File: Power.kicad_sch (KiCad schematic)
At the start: 18 parts, among them J4 Conn_01x02, SW2 SW_Push, U6 NPM1300-QEAA-R7

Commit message: Layout V1
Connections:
- net VSET2: now reaches R13.1, U6.16 (VSET2)
- net VSET1: now reaches R12.1, U6.17 (VSET1)
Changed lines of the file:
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@@
+		)
+	)
+	(label "VSET2"
+		(at 87.63 118.11 0)
+		(effects
+			(font
+				(size 1.27 1.27)
+			)
+			(justify left bottom)
 		)
 	)
@@
 		)
 	)
+	(label "VSET1"
+		(at 87.63 115.57 0)
+		(effects
+			(font
+				(size 1.27 1.27)
+			)
+			(justify left bottom)
+		)
+	)

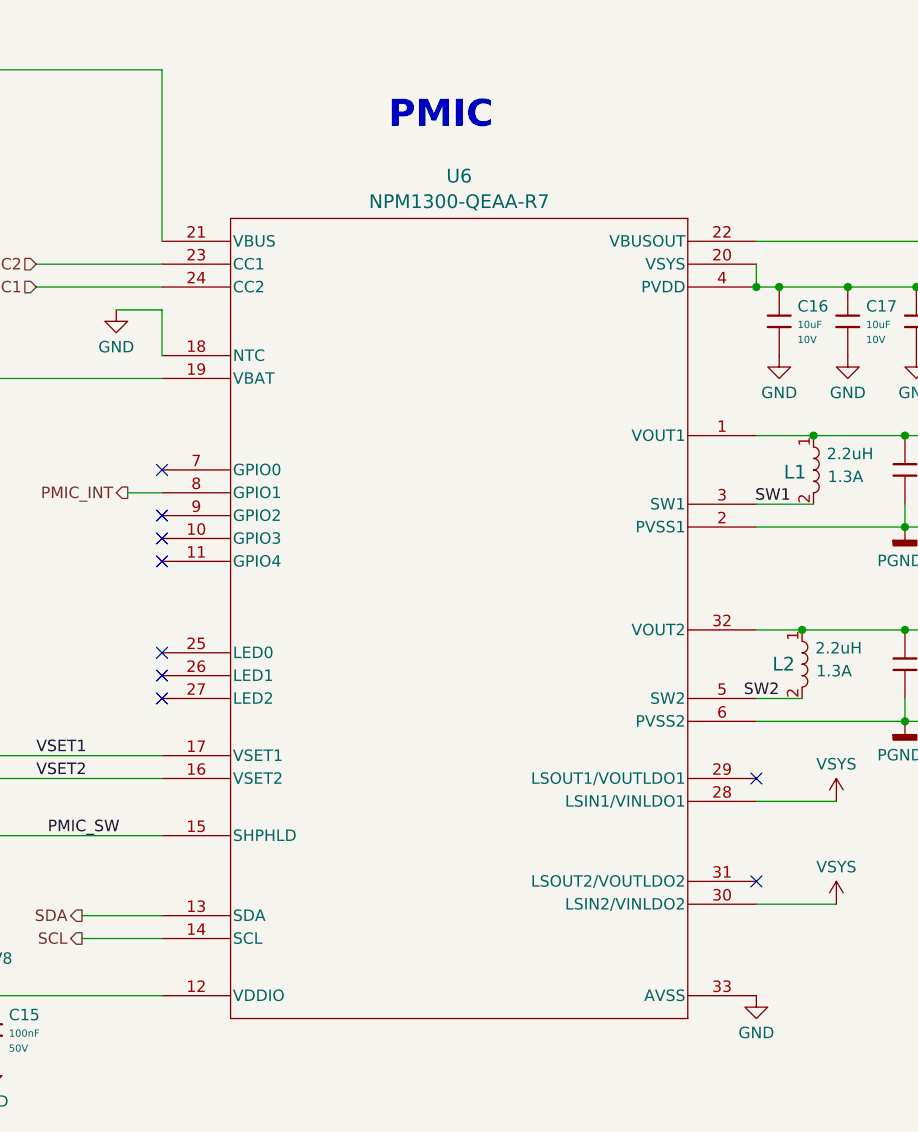
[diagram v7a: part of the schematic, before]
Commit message: Update most sym/footprint libraries
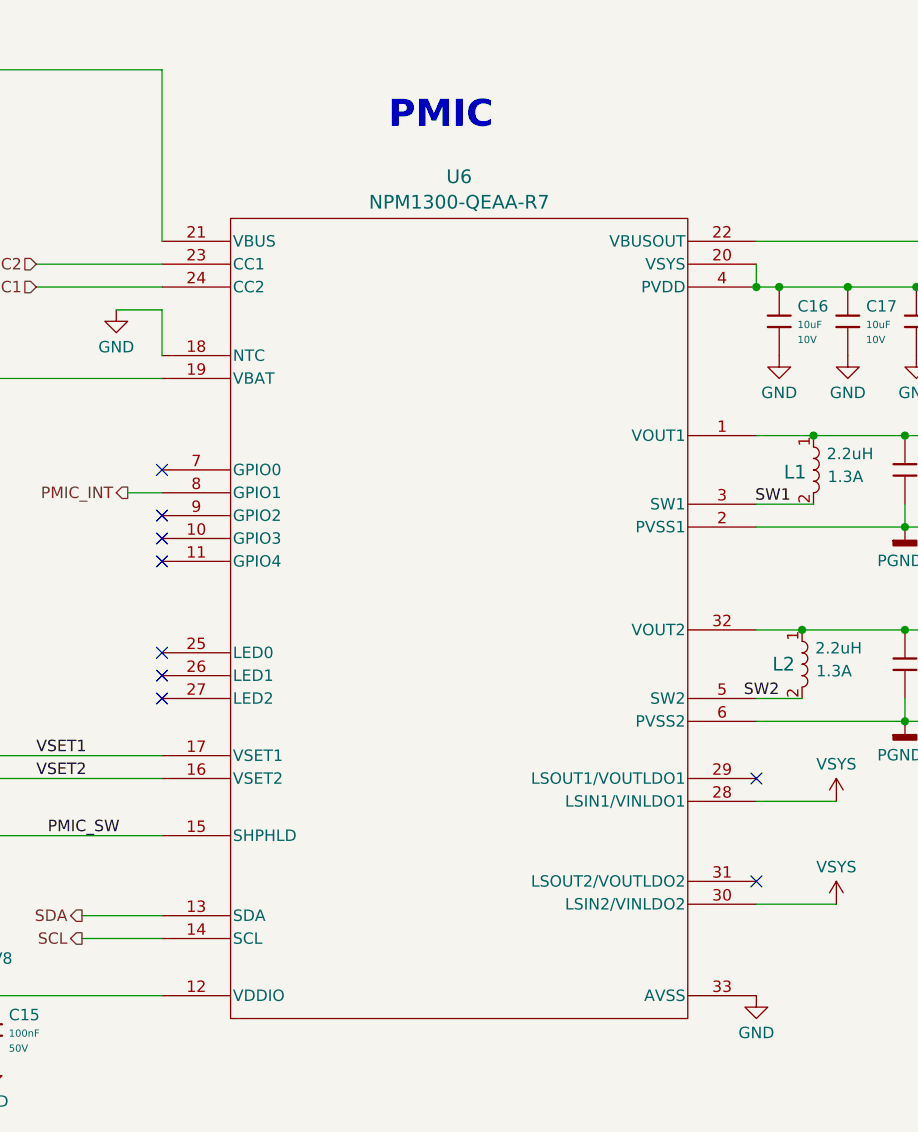
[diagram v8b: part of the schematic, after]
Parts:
- removed U6: NPM1300-QEAA-R7, NPM:QFN32_5X5_NOR, symbol 2026-04-08_23-52-45:NPM1300-QEAA-R7
- added U6: NPM1300-QEAA-R7, Smart_Watch:QFN32_5X5_NOR-L, symbol Smart_Watch:NPM1300-QEAA-R7
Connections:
- net +1V8: now also U6.1 (VOUT1), U6.12 (VDDIO)
- net +3V0: now also U6.32 (VOUT2)
- net +BATT: now also U6.19 (VBAT)
- net CC1: now also U6.24 (CC2)
- net CC2: now also U6.23 (CC1)
- net GND: now also U6.18 (NTC), U6.33 (AVSS)
- net PGND1: now also U6.2 (PVSS1)
- net PGND2: now also U6.6 (PVSS2)
- net PMIC_INT: now also U6.8 (GPIO1)
- net PMIC_SW: now also U6.15 (SHPHLD)
- net SCL: now also U6.14 (SCL)
- net SDA: now also U6.13 (SDA)
- net SW1: now also U6.3 (SW1)
- net SW2: now also U6.5 (SW2)
- net VBUS_IN: now also U6.21 (VBUS)
- net VBUS_OUT: now also U6.22 (VBUSOUT)
- net VSET1: now also U6.17 (VSET1)
- net VSET2: now also U6.16 (VSET2)
- net VSYS: now also U6.20 (VSYS), U6.28 (LSIN1/VINLDO1), U6.30 (LSIN2/VINLDO2), U6.4 (PVDD)
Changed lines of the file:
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@@
+	)
+	(symbol
+		(lib_id "Smart_Watch:NPM1300-QEAA-R7")
+		(at 134.62 100.33 0)
+		(unit 1)
+		(body_style 1)
+		(exclude_from_sim no)
+		(in_bom yes)
+		(on_board yes)
+		(in_pos_files yes)
+		(dnp no)
+		(fields_autoplaced yes)
+		(property "Reference" "U6"
+			(at 134.62 51.2496 0)
+			(show_name no)
+			(do_not_autoplace no)
+			(effects
+				(font
+					(size 1.524 1.524)
+				)
+			)
+		)
+		(property "Value" "NPM1300-QEAA-R7"
+			(at 134.62 54.0825 0)
+			(show_name no)
+			(do_not_autoplace no)
+			(effects
+				(font
+					(size 1.524 1.524)
+				)
+			)
+		)
+		(property "Footprint" "Smart_Watch:QFN32_5X5_NOR-L"
+			(at 134.112 39.878 0)
+			(hide yes)
+			(show_name yes)
+			(do_not_autoplace no)
+			(effects
+				(font
+					(size 1.27 1.27)
+				)
+			)
+		)
+		(property "Datasheet" "NPM1300-QEAA-R7"
+			(at 133.858 44.196 0)
+			(hide yes)
+			(show_name yes)
+			(do_not_autoplace no)
+			(effects
+				(font
+					(size 1.27 1.27)
+				)
+			)
+		)
+		(property "Description" ""
+			(at 132.842 42.418 0)
+			(hide yes)
+			(show_name yes)
+			(do_not_autoplace no)
+			(effects
+				(font
+					(size 1.27 1.27)
+				)
+			)
+		)
+		(pin "7"
+		)
+		(pin "13"
+		)
+		(pin "1"
+		)
+		(pin "3"
+		)
+		(pin "6"
+		)
+		(pin "11"
+		)
+		(pin "19"
+		)
+		(pin "9"
+		)
+		(pin "17"
+		)
+		(pin "2"
+		)
+		(pin "20"
+		)
+		(pin "8"
+		)
+		(pin "10"
+		)
+		(pin "12"
+		)
+		(pin "15"
+		)
+		(pin "16"
+		)
+		(pin "4"
+		)
+		(pin "5"
+		)
+		(pin "14"
+		)
+		(pin "18"
+		)
+		(pin "23"
+		)
+		(pin "24"
+		)
+		(pin "25"
+		)
+		(pin "21"
+		)
+		(pin "26"
+		)
+		(pin "27"
+		)
+		(pin "22"
+		)
+		(pin "28"
+		)
+		(pin "29"
+		)
+		(pin "31"
+		)
+		(pin "33"
+		)
+		(pin "30"
+		)
+		(pin "32"
+		)
+		(instances
+			(project "Smart_Watch"
+				(path "/69095a4d-0a57-4fa3-aecb-1cfd89eedc11/bed567dd-6d09-419a-b99a-3e57c9439bd4/88559da1-41ec-4d01-a245-44d6dbccae3b"
+					(reference "U6")
+					(unit 1)
+				)
+			)
+		)
 	)
 	(symbol
@@
 				)
 			)
-		)
-	)
-	(symbol
-		(lib_id "2026-04-08_23-52-45:NPM1300-QEAA-R7")
-		(at 101.6 60.96 0)
-		(unit 1)
-		(body_style 1)
-		(exclude_from_sim no)
-		(in_bom yes)
-		(on_board yes)
-		(in_pos_files yes)
-		(dnp no)
-		(fields_autoplaced yes)
-		(property "Reference" "U6"
-			(at 134.62 51.1861 0)
-			(show_name no)
-			(do_not_autoplace no)
-			(effects
-				(font
-					(size 1.524 1.524)
-				)
-			)
-		)
-		(property "Value" "NPM1300-QEAA-R7"
-			(at 134.62 54.019 0)
-			(show_name no)
-			(do_not_autoplace no)
-			(effects
-				(font
-					(size 1.524 1.524)
-				)
-			)
-		)
-		(property "Footprint" "NPM:QFN32_5X5_NOR"
-			(at 101.6 60.96 0)
-			(hide yes)
-			(show_name no)
-			(do_not_autoplace no)
-			(effects
-				(font
-					(size 1.27 1.27)
-					(italic yes)
-				)
-			)
-		)
-		(property "Datasheet" "NPM1300-QEAA-R7"
-			(at 101.6 60.96 0)
-			(hide yes)
-			(show_name no)
-			(do_not_autoplace no)
-			(effects
-				(font
-					(size 1.27 1.27)
-					(italic yes)
-				)
-			)
-		)
-		(property "Description" ""
-			(at 101.6 60.96 0)
-			(hide yes)
-			(show_name no)
-			(do_not_autoplace no)
-			(effects
-				(font
-					(size 1.27 1.27)
-				)
-			)
-		)
-		(pin "4"
-		)
-		(pin "33"
-		)
-		(pin "28"
-		)
-		(pin "24"
-		)
-		(pin "2"
-		)
-		(pin "21"
-		)
-		(pin "19"
-		)
-		(pin "1"
-		)
-		(pin "7"
-		)
-		(pin "16"
-		)
-		(pin "29"
-		)
-		(pin "12"
-		)
-		(pin "6"
-		)
-		(pin "8"
-		)
-		(pin "13"
-		)
-		(pin "15"
-		)
-		(pin "31"
-		)
-		(pin "3"
-		)
-		(pin "30"
-		)
-		(pin "27"
-		)
-		(pin "25"
-		)
-		(pin "10"
-		)
-		(pin "5"
-		)
-		(pin "9"
-		)
-		(pin "14"
-		)
-		(pin "11"
-		)
-		(pin "32"
-		)
-		(pin "26"
-		)
-		(pin "23"
-		)
-		(pin "22"
-		)
-		(pin "20"
-		)
-		(pin "17"
-		)
-		(pin "18"
-		)
-		(instances
-			(project "Smart_Watch"
-				(path "/69095a4d-0a57-4fa3-aecb-1cfd89eedc11/bed567dd-6d09-419a-b99a-3e57c9439bd4/88559da1-41ec-4d01-a245-44d6dbccae3b"
-					(reference "U6")
-					(unit 1)
-					(variant
-						(name "No Trans")
-					)
-					(variant
-						(name "W Trans")
-					)
-				)
-			)
